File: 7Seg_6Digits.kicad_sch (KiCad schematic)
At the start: 12 parts, among them U1 DA56-11SURKWA, U2 DA56-11SURKWA, U3 DA56-11SURKWA, U4 ULN2003, U5 4543

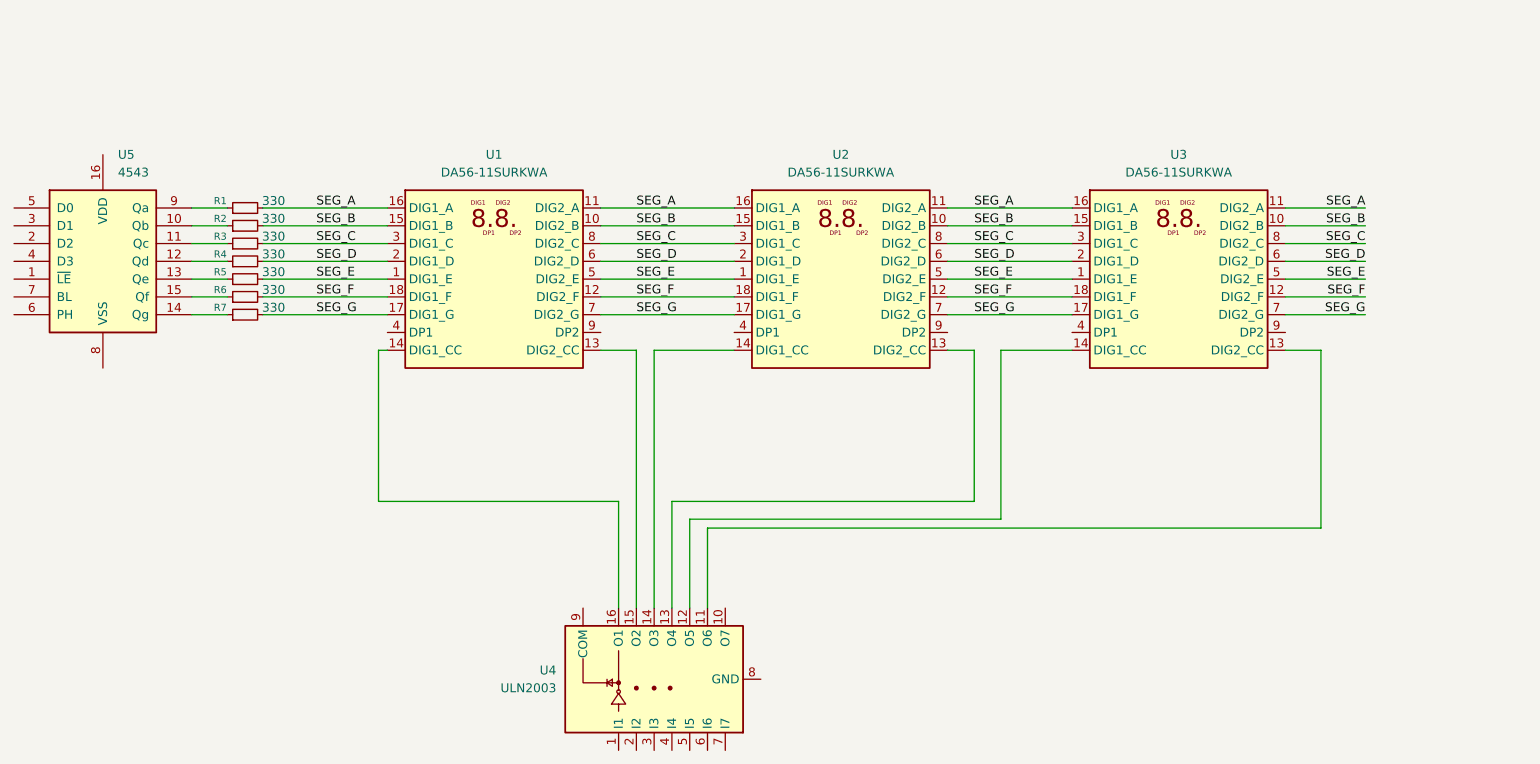
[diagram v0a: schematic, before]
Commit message: Refactor code structure for improved readability and maintainability
add Top lecvel and 6 Digits view
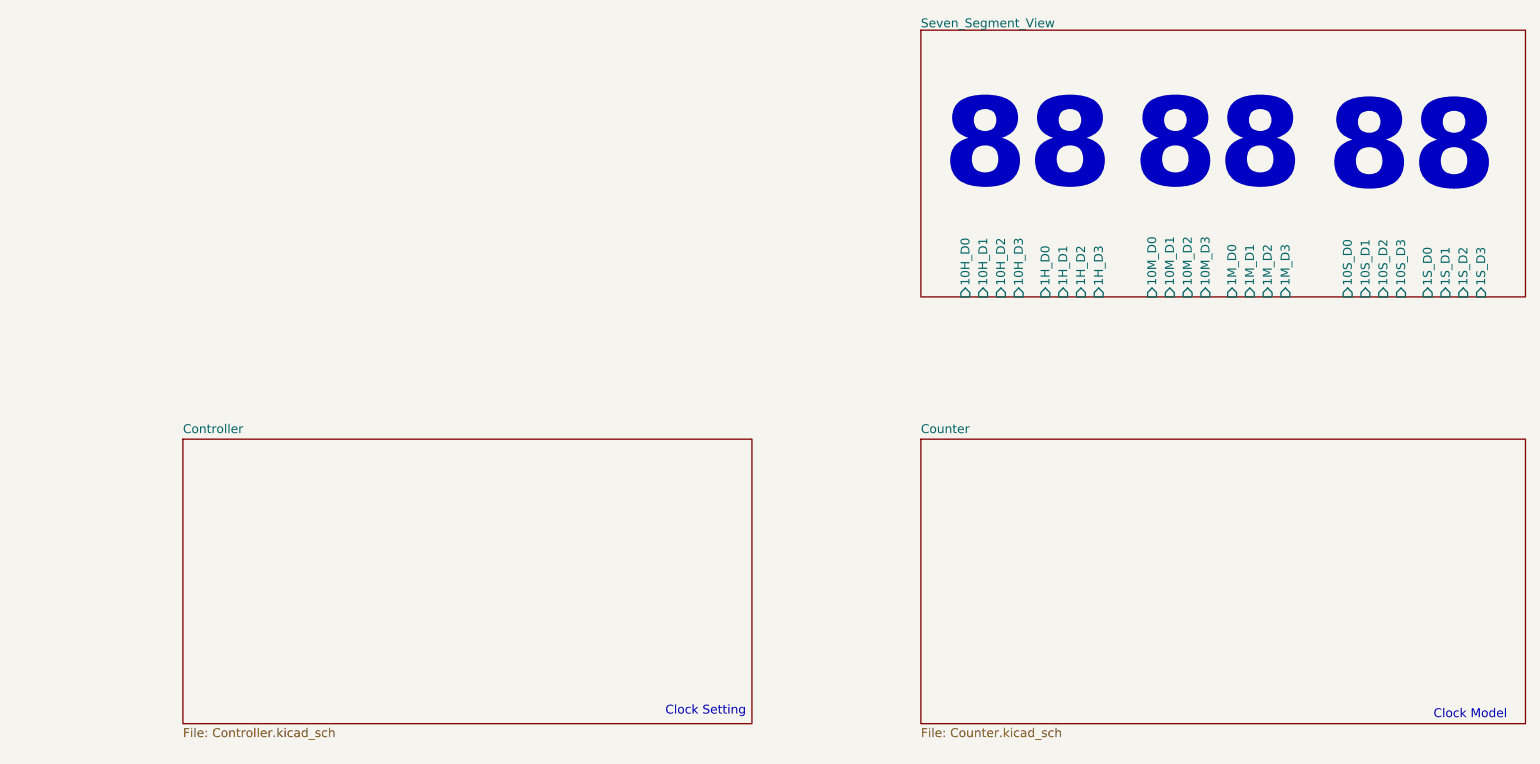
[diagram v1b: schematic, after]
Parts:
- removed R1, R2, R3, R4, R5, R6, R7: 330, symbol Device:R_Small
- removed U1, U2, U3: DA56-11SURKWA, Display_7Segment:DA56-11CGKWA, symbol Display_Character:DC56-11CGKWA
- removed U4: ULN2003, symbol Transistor_Array:ULN2003
- removed U5: 4543, symbol 4xxx:4543
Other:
- added sheet Controller (Controller.kicad_sch)
- added sheet Counter (Counter.kicad_sch)
- added sheet Seven_Segment_View (Seven_Segment_View.kicad_sch)
- note added: "88"
- note added: "Clock Model"
- note added: "Clock Setting"
